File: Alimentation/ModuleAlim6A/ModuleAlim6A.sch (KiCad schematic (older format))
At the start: 19 parts, among them J1 Conn_01x05, J2 Conn_01x02, J3 OUTPUT, U1 PTN78020W_EUK-7, U2 ACS712xLCTR-20A

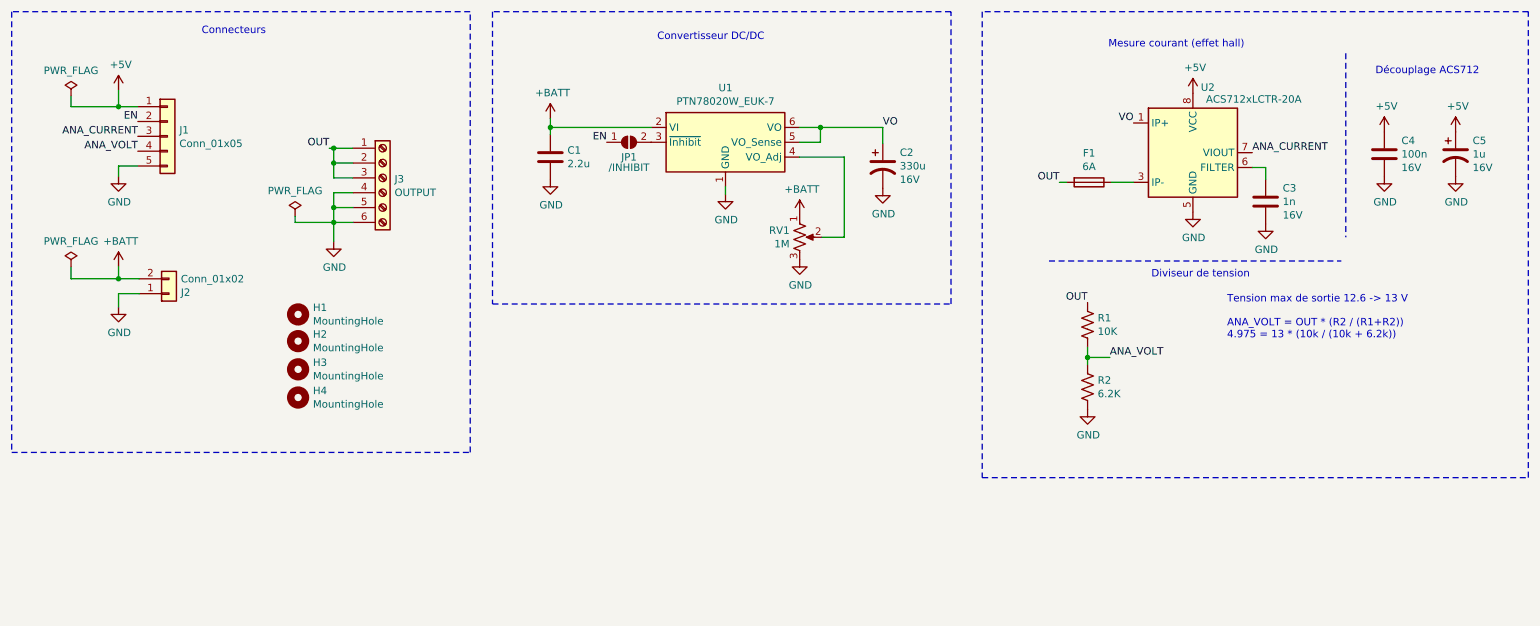
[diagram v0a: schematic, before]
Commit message: Module alim ISO, clean master alim
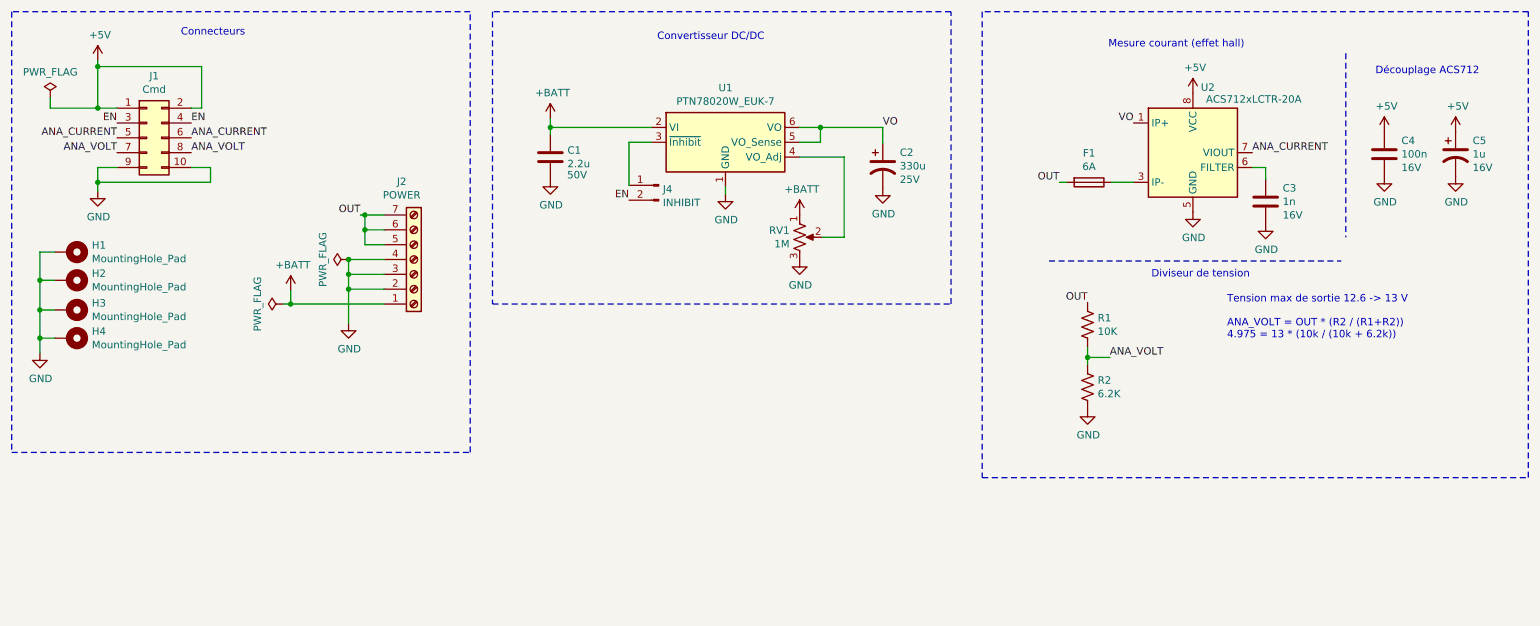
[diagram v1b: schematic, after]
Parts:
- removed H1, H2, H3, H4: MountingHole, MountingHole:MountingHole_3.2mm_M3, symbol Mechanical:MountingHole
- removed J1: Conn_01x05, Connector_JST:JST_PH_B5B-PH-K_1x05_P2.00mm_Vertical, symbol Connector_Generic:Conn_01x05
- removed J2: Conn_01x02, Connector_Phoenix_MC_HighVoltage:PhoenixContact_MC_1,5_2-G-5.08_1x02_P5.08mm_Horizontal, symbol Connector_Generic:Conn_01x02
- removed J3: OUTPUT, TerminalBlock_Phoenix:TerminalBlock_Phoenix_PT-1,5-6-5.0-H_1x06_P5.00mm_Horizontal, symbol Connector:Screw_Terminal_01x06
- removed JP1: /INHIBIT, Jumper:SolderJumper-2_P1.3mm_Open_RoundedPad1.0x1.5mm, symbol Jumper:SolderJumper_2_Open
- added H1, H2, H3, H4: MountingHole_Pad, MountingHole:MountingHole_3.2mm_M3_Pad_Via, symbol Mechanical:MountingHole_Pad
- added J1: Cmd, Connector_IDC:IDC-Header_2x05_P2.54mm_Vertical, symbol Connector_Generic:Conn_02x05_Odd_Even
- added J2: POWER, TerminalBlock_Phoenix:TerminalBlock_Phoenix_MKDS-1,5-7-5.08_1x07_P5.08mm_Horizontal, symbol Connector:Screw_Terminal_01x07
- added J4: INHIBIT, Connector_PinHeader_2.54mm:PinHeader_1x02_P2.54mm_Vertical, symbol Connector:Conn_01x02_Male
- C1: footprint Capacitor_SMD:C_0805_2012Metric_Pad1.18x1.45mm_HandSolder -> Capacitor_SMD:C_1206_3216Metric_Pad1.33x1.80mm_HandSolder; LCSC Part (none) -> C282852; Tension (none) -> 50V
- C2: footprint Capacitor_SMD:CP_Elec_10x10 -> Capacitor_SMD:CP_Elec_8x10; LCSC Part (none) -> C249647; Tension 16V -> 25V
- C3: LCSC Part (none) -> C163169
- C4: footprint Capacitor_SMD:C_0805_2012Metric_Pad1.18x1.45mm_HandSolder -> Capacitor_SMD:C_0603_1608Metric_Pad1.08x0.95mm_HandSolder; LCSC Part (none) -> C80516
- C5: LCSC Part (none) -> C249445
- F1, U1: JLCPCB BOM (none) -> 0
- R1: LCSC Part (none) -> C191317
- R2: LCSC Part (none) -> C413691
- RV1: footprint Potentiometer_SMD:Potentiometer_Bourns_TC33X_Vertical -> Potentiometer_THT:Potentiometer_Bourns_3266Y_Vertical; JLCPCB BOM (none) -> 0
- U2: LCSC Part (none) -> C10681
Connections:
- net +5V: now also J1.1 (Pin_1), J1.2 (Pin_2)
- net +BATT: now also J2.1 (Pin_1)
- net ANA_CURRENT: now also J1.5 (Pin_5), J1.6 (Pin_6)
- net ANA_VOLT: now also J1.7 (Pin_7), J1.8 (Pin_8)
- net EN: now also J1.3 (Pin_3), J1.4 (Pin_4), J4.2 (Pin_2)
- net GND: now also H1.1, H2.1, H3.1, H4.1, J1.10 (Pin_10), J1.9 (Pin_9), J2.2 (Pin_2), J2.3 (Pin_3), J2.4 (Pin_4)
- net OUT: now also J2.5 (Pin_5), J2.6 (Pin_6), J2.7 (Pin_7)
- net at U1.3 (~Inhibit): now also J4.1 (Pin_1)

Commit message: Modules Alim 3A et 6A uniforme sans mesure courant/tension
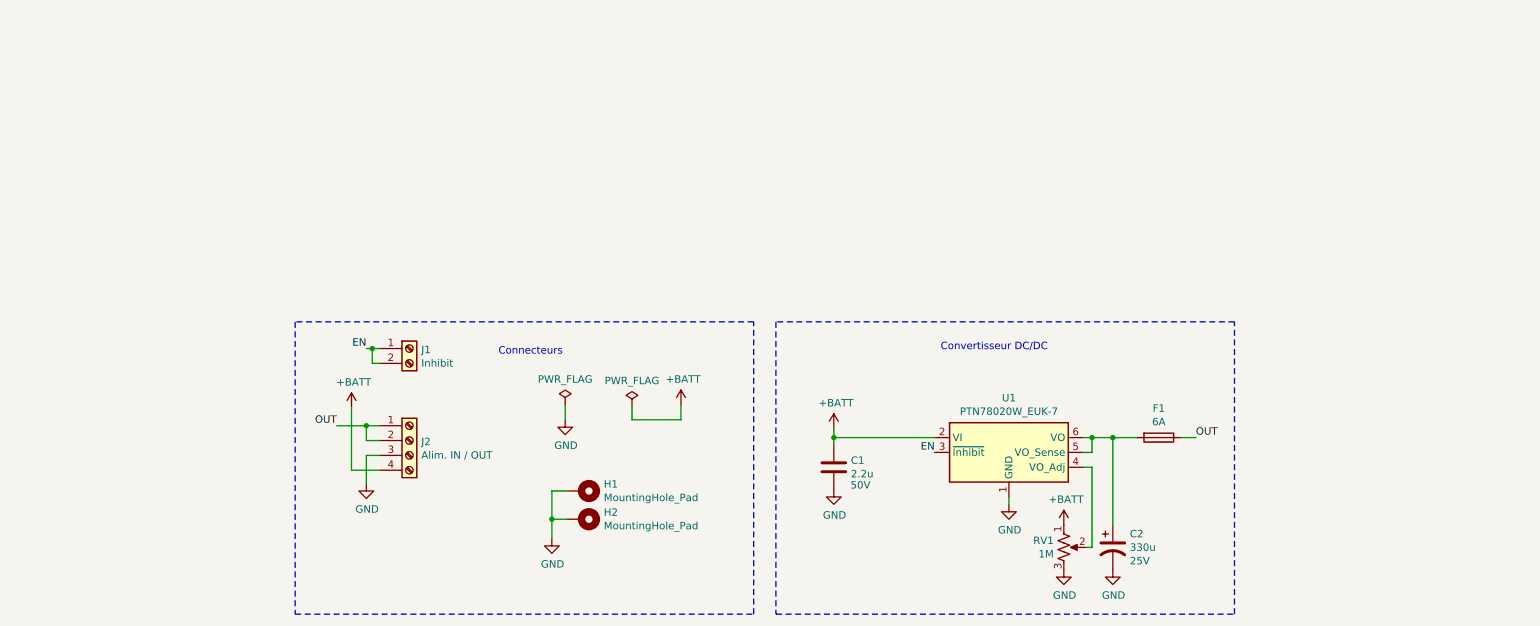
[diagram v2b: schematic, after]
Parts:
- removed C3: 1n, Capacitor_SMD:C_0603_1608Metric_Pad1.08x0.95mm_HandSolder, symbol Device:C
- removed C4: 100n, Capacitor_SMD:C_0603_1608Metric_Pad1.08x0.95mm_HandSolder, symbol Device:C
- removed C5: 1u, Capacitor_SMD:CP_Elec_4x5.3, symbol Device:CP1
- removed H3, H4: MountingHole_Pad, MountingHole:MountingHole_3.2mm_M3_Pad_Via, symbol Mechanical:MountingHole_Pad
- removed J1: Cmd, Connector_IDC:IDC-Header_2x05_P2.54mm_Vertical, symbol Connector_Generic:Conn_02x05_Odd_Even
- removed J2: POWER, TerminalBlock_Phoenix:TerminalBlock_Phoenix_MKDS-1,5-7-5.08_1x07_P5.08mm_Horizontal, symbol Connector:Screw_Terminal_01x07
- removed J4: INHIBIT, Connector_PinHeader_2.54mm:PinHeader_1x02_P2.54mm_Vertical, symbol Connector:Conn_01x02_Male
- removed R1: 10K, Resistor_SMD:R_0805_2012Metric_Pad1.20x1.40mm_HandSolder, symbol Device:R_US
- removed R2: 6.2K, Resistor_SMD:R_0805_2012Metric_Pad1.20x1.40mm_HandSolder, symbol Device:R_US
- removed U2: ACS712xLCTR-20A, Package_SO:SOIC-8_3.9x4.9mm_P1.27mm, symbol Sensor_Current:ACS712xLCTR-20A
- added J1: Inhibit, TerminalBlock_Phoenix:TerminalBlock_Phoenix_MPT-0,5-2-2.54_1x02_P2.54mm_Horizontal, symbol Connector:Screw_Terminal_01x02
- added J2: Alim. IN / OUT, TerminalBlock_Phoenix:TerminalBlock_Phoenix_MKDS-1,5-4-5.08_1x04_P5.08mm_Horizontal, symbol Connector:Screw_Terminal_01x04
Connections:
- net +BATT: now also J2.4 (Pin_4)
- net EN: now also U1.3 (~Inhibit), J1.1 (Pin_1), J1.2 (Pin_2)
- net GND: now also J2.3 (Pin_3)
- net OUT: now also F1.1, J2.1 (Pin_1), J2.2 (Pin_2); no longer F1.2
- net VO: no longer names the net of C2.1, U1.5 (VO_Sense), U1.6 (VO)
- net VO: now also F1.2
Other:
- note removed: "Diviseur de tension"
- note removed: "Découplage ACS712"
- note removed: "Mesure courant (effet hall)"
- note removed: "Tension max de sortie 12.6 -> 13 V\n\nANA_VOLT = OUT * (R2 / (R1+R2))\n4.975 = 13 * (10k / (10k + 6.2k))"
- moved on the sheet: C1, C2, F1, H1, H2, RV1, U1

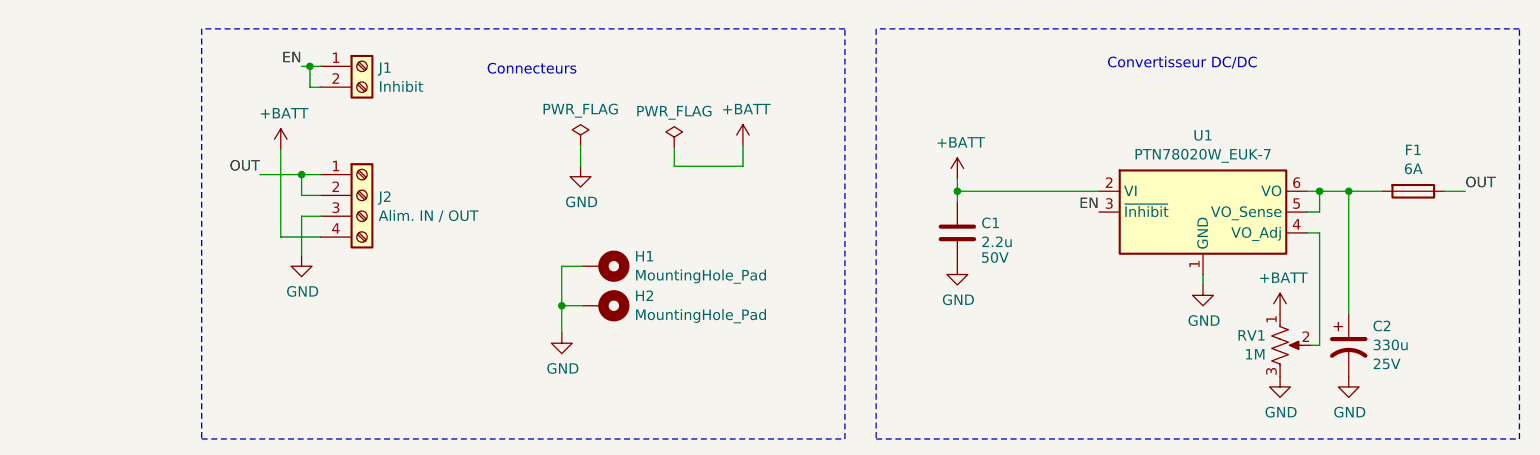
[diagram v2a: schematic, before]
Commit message: Finalisation modules 3A et 6A, routage master alim
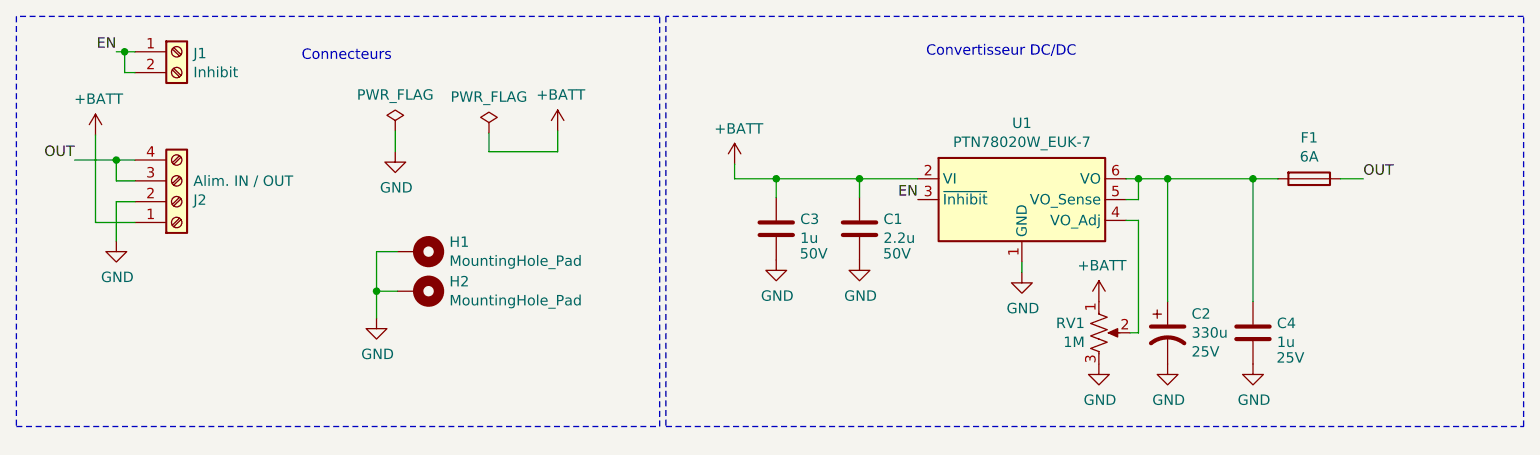
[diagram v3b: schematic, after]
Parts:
- added C3: 1u, Capacitor_SMD:C_0603_1608Metric_Pad1.08x0.95mm_HandSolder, symbol Device:C
- added C4: 1u, Capacitor_SMD:C_0402_1005Metric_Pad0.74x0.62mm_HandSolder, symbol Device:C
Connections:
- net +BATT: now also J2.1 (Pin_1), C3.1; no longer J2.4 (Pin_4)
- net GND: now also J2.2 (Pin_2), C3.2, C4.2; no longer J2.3 (Pin_3)
- net OUT: now also J2.3 (Pin_3), J2.4 (Pin_4); no longer J2.1 (Pin_1), J2.2 (Pin_2)
- net at C2.1, F1.2, U1.5 (VO_Sense)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: now also C4.1
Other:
- moved on the sheet: C1, C2, F1, H1, H2, J1, J2, RV1, U1

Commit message: Finalisation pour commande pack Alimentation 14/02/2021
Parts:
- C1: LCSC Part C282852 -> C50254
- C2: LCSC Part C249647 -> C134842
- C3: footprint Capacitor_SMD:C_0603_1608Metric_Pad1.08x0.95mm_HandSolder -> Capacitor_SMD:C_0805_2012Metric_Pad1.18x1.45mm_HandSolder; LCSC Part C105174 -> C28323
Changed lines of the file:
@@
 F 3 "~" H 7220 4240 50  0001 C CNN
 F 4 "25V" H 7335 4149 50  0000 L CNN "Tension"
-F 5 "C249647" H 7220 4240 50  0001 C CNN "LCSC Part"
+F 5 "C134842" H 7220 4240 50  0001 C CNN "LCSC Part"
 	1    7220 4240
 	1    0    0    -1
@@
 F 3 "~" H 5740 3740 50  0001 C CNN
 F 4 "50V" H 5920 3620 50  0000 C CNN "Tension"
-F 5 "C282852" H 5740 3740 50  0001 C CNN "LCSC Part"
+F 5 "C50254" H 5740 3740 50  0001 C CNN "LCSC Part"
 	1    5740 3740
 	1    0    0    -1
@@
 F 0 "C3" H 5455 3786 50  0000 L CNN
 F 1 "1u" H 5455 3695 50  0000 L CNN
-F 2 "Capacitor_SMD:C_0603_1608Metric_Pad1.08x0.95mm_HandSolder" H 5378 3590 50  0001 C CNN
+F 2 "Capacitor_SMD:C_0805_2012Metric_Pad1.18x1.45mm_HandSolder" H 5378 3590 50  0001 C CNN
 F 3 "~" H 5340 3740 50  0001 C CNN
 F 4 "50V" H 5520 3620 50  0000 C CNN "Tension"
-F 5 "C105174" H 5340 3740 50  0001 C CNN "LCSC Part"
+F 5 "C28323" H 5340 3740 50  0001 C CNN "LCSC Part"
 	1    5340 3740
 	1    0    0    -1
